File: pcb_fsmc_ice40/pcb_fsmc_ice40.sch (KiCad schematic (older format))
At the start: 42 parts, among them P1 SD_CARD, P2 CONN_02X20, P5 CONN_02X12, P7 KNUSB, SW1 SWITCH_INV, U1 STM32F40X_LQFP144, X1 CRYSTAL

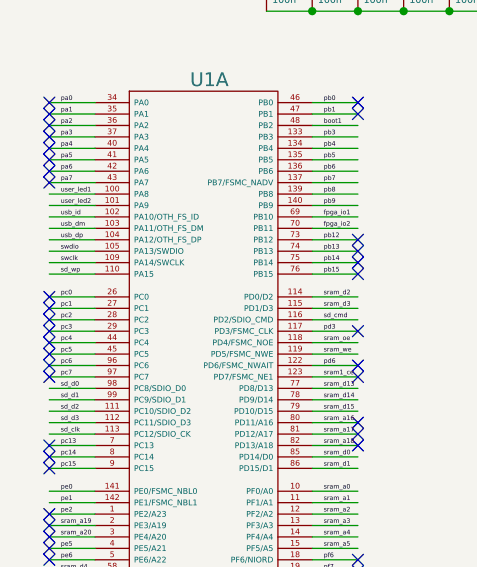
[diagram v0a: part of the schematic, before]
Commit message: Connect PA9 to usb_5v, as used by some ST library code.
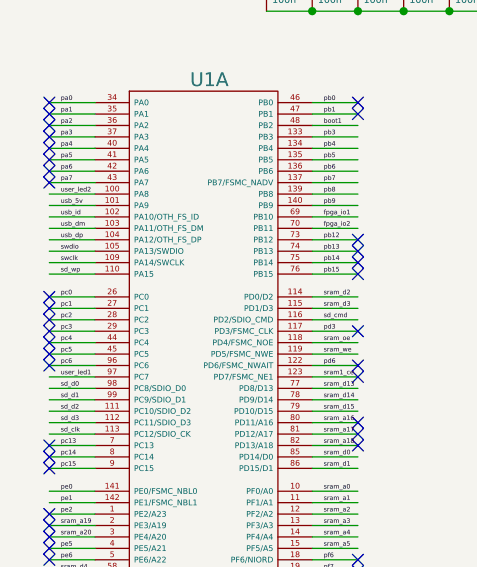
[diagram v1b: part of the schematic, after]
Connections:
- net labels removed: pc7
- no-connect marks 58 -> 57
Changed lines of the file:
@@
 	1    0    0    -1
 $EndComp
-Text Label 950  2450 0    20   ~ 0
-pc7
 Text Label 950  2400 0    20   ~ 0
 pc6
@@
 Text Label 950  1750 0    20   ~ 0
 usb_id
-Text Label 950  1700 0    20   ~ 0
+Text Label 950  1650 0    20   ~ 0
 user_led2
-Text Label 950  1650 0    20   ~ 0
+Text Label 950  2450 0    20   ~ 0
 user_led1
 Text Label 950  1600 0    20   ~ 0
@@
 NoConn ~ 900  2350
 NoConn ~ 900  2400
-NoConn ~ 900  2450
 NoConn ~ 900  2750
 NoConn ~ 900  2800
@@
 NoConn ~ 2250 1900
 NoConn ~ 8975 1400
+Text Label 950  1700 0    20   ~ 0
+usb_5v
 $EndSCHEMATC
